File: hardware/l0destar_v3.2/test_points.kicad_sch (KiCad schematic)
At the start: 9 parts

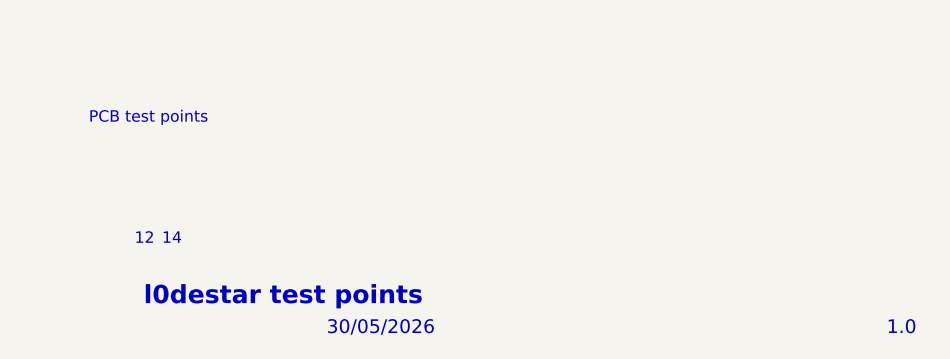
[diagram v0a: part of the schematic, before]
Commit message: update sheet annotations
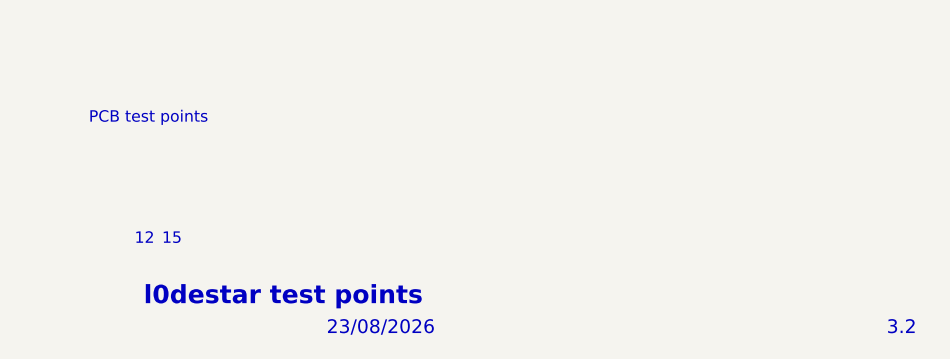
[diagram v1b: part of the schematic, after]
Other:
- note added: "15"
- note added: "23/08/2026"
- note added: "3.2"
- note removed: "1.0"
- note removed: "14"
- note removed: "30/05/2026"
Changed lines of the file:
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@@
 		)
 	)
-	(text "1.0"
+	(text "3.2"
 		(exclude_from_sim no)
 		(at 268.478 193.294 0)
@@
 		)
 	)
-	(text "30/05/2026"
+	(text "23/08/2026"
 		(exclude_from_sim no)
 		(at 206.248 193.294 0)
@@
 		)
 	)
-	(text "14"
+	(text "15"
 		(exclude_from_sim no)
 		(at 187.96 183.388 0)
